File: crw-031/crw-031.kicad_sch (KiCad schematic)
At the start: 37 parts, among them J1 PICKIT, J2 L, J3 R, J4 USB_C_Receptacle_USB2.0_16P, SW1 BOOT, SW2 RESET, U1 PIC32MX250F128D-IPT, U2 USBLC6-2SC6, U3 MCP1703Ax-500xxDB, U4 MCP1703Ax-330xxTT, Y1 8MHz

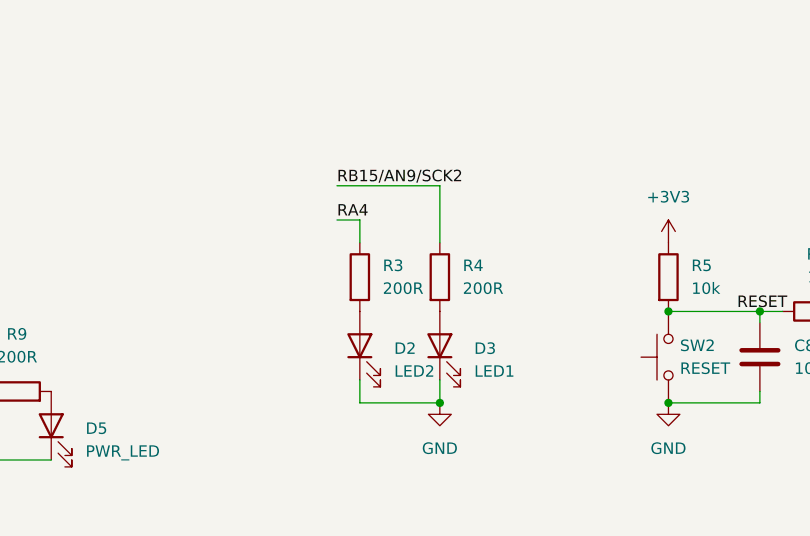
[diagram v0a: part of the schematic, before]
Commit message: Tweak FMini
- FIx LED footprints
- move stuff around in schematic
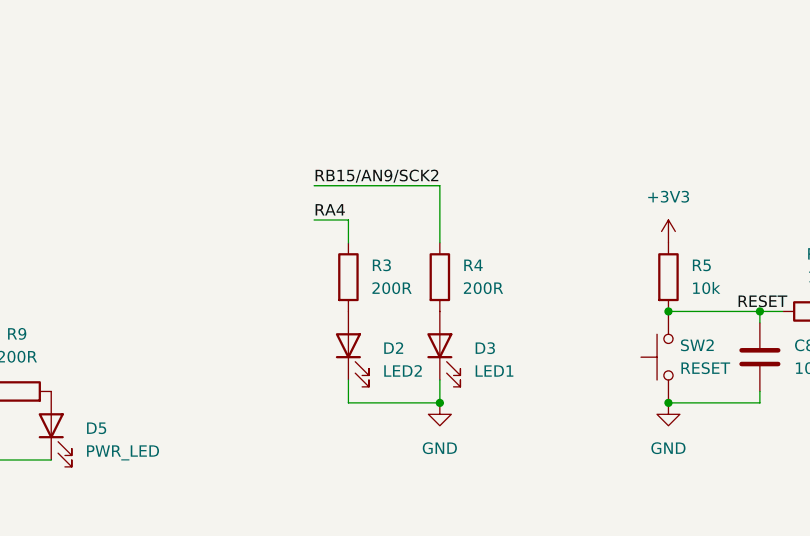
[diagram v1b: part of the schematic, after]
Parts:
- D2, D3, D5: footprint Diode_SMD:D_0603_1608Metric -> LED_SMD:LED_0603_1608Metric
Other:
- moved on the sheet: D2, R3
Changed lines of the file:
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@@
 	(title_block
 		(title "Flinduino Mini")
+		(date "2024-07-27")
+		(rev "A")
 	)
 	(junction
@@
 	(wire
 		(pts
-			(xy 186.69 154.94) (xy 189.23 154.94)
+			(xy 184.15 154.94) (xy 187.96 154.94)
 		)
 		(stroke
@@
 	(wire
 		(pts
-			(xy 186.69 151.13) (xy 198.12 151.13)
+			(xy 184.15 151.13) (xy 198.12 151.13)
 		)
 		(stroke
@@
 	(wire
 		(pts
-			(xy 189.23 154.94) (xy 189.23 157.48)
+			(xy 187.96 154.94) (xy 187.96 157.48)
 		)
 		(stroke
@@
 	(wire
 		(pts
-			(xy 189.23 172.72) (xy 189.23 175.26)
+			(xy 187.96 172.72) (xy 187.96 175.26)
 		)
 		(stroke
@@
 	(wire
 		(pts
-			(xy 189.23 175.26) (xy 198.12 175.26)
+			(xy 187.96 175.26) (xy 198.12 175.26)
 		)
 		(stroke
@@
 	)
 	(label "RB15{slash}AN9{slash}SCK2"
-		(at 186.69 151.13 0)
+		(at 184.15 151.13 0)
 		(fields_autoplaced yes)
 		(effects
@@
 	)
 	(label "RA4"
-		(at 186.69 154.94 0)
+		(at 184.15 154.94 0)
 		(fields_autoplaced yes)
 		(effects
@@
 	(symbol
 		(lib_id "Device:R")
-		(at 189.23 161.29 0)
+		(at 187.96 161.29 0)
 		(unit 1)
 		(exclude_from_sim no)
@@
 		(fields_autoplaced yes)
 		(property "Reference" "R3"
-			(at 191.77 160.0199 0)
+			(at 190.5 160.0199 0)
 			(effects
 				(font
@@
 		)
 		(property "Value" "200R"
-			(at 191.77 162.5599 0)
+			(at 190.5 162.5599 0)
 			(effects
 				(font
@@
 		)
 		(property "Footprint" "Resistor_SMD:R_0603_1608Metric"
-			(at 187.452 161.29 90)
+			(at 186.182 161.29 90)
 			(effects
 				(font
@@
 		)
 		(property "Datasheet" "~"
-			(at 189.23 161.29 0)
+			(at 187.96 161.29 0)
 			(effects
 				(font
@@
 		)
 		(property "Description" "Resistor"
-			(at 189.23 161.29 0)
+			(at 187.96 161.29 0)
 			(effects
 				(font
@@
 	(symbol
 		(lib_id "Device:LED")
-		(at 189.23 168.91 90)
+		(at 187.96 168.91 90)
 		(unit 1)
 		(exclude_from_sim no)
@@
 		(fields_autoplaced yes)
 		(property "Reference" "D2"
-			(at 193.04 169.2274 90)
+			(at 191.77 169.2274 90)
 			(effects
 				(font
@@
 		)
 		(property "Value" "LED2"
-			(at 193.04 171.7674 90)
+			(at 191.77 171.7674 90)
 			(effects
 				(font
@@
 			)
 		)
-		(property "Footprint" "Diode_SMD:D_0603_1608Metric"
-			(at 189.23 168.91 0)
+		(property "Footprint" "LED_SMD:LED_0603_1608Metric"
+			(at 187.96 168.91 0)
 			(effects
 				(font
@@
 		)
 		(property "Datasheet" "~"
-			(at 189.23 168.91 0)
+			(at 187.96 168.91 0)
 			(effects
 				(font
@@
 		)
 		(property "Description" "Light emitting diode"
-			(at 189.23 168.91 0)
+			(at 187.96 168.91 0)
 			(effects
 				(font
@@
 			)
 		)
-		(property "Footprint" "Diode_SMD:D_0603_1608Metric"
+		(property "Footprint" "LED_SMD:LED_0603_1608Metric"
 			(at 154.94 177.8 0)
 			(effects
@@
 			)
 		)
-		(property "Footprint" "Diode_SMD:D_0603_1608Metric"
+		(property "Footprint" "LED_SMD:LED_0603_1608Metric"
 			(at 198.12 168.91 0)
 			(effects
